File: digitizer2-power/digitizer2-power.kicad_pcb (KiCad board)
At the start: 2 copper layers, 25 x 40 mm, 37 parts, among them P1 CONN_01X02, P2 CONN_01X05, Q1 Q_NPN_BEC, Q2 Q_NPN_BEC, U1 LM3674, U2 LM3671MF-1.8, U3 LM3671MF-1.5, U4 LM3671MF-3.3

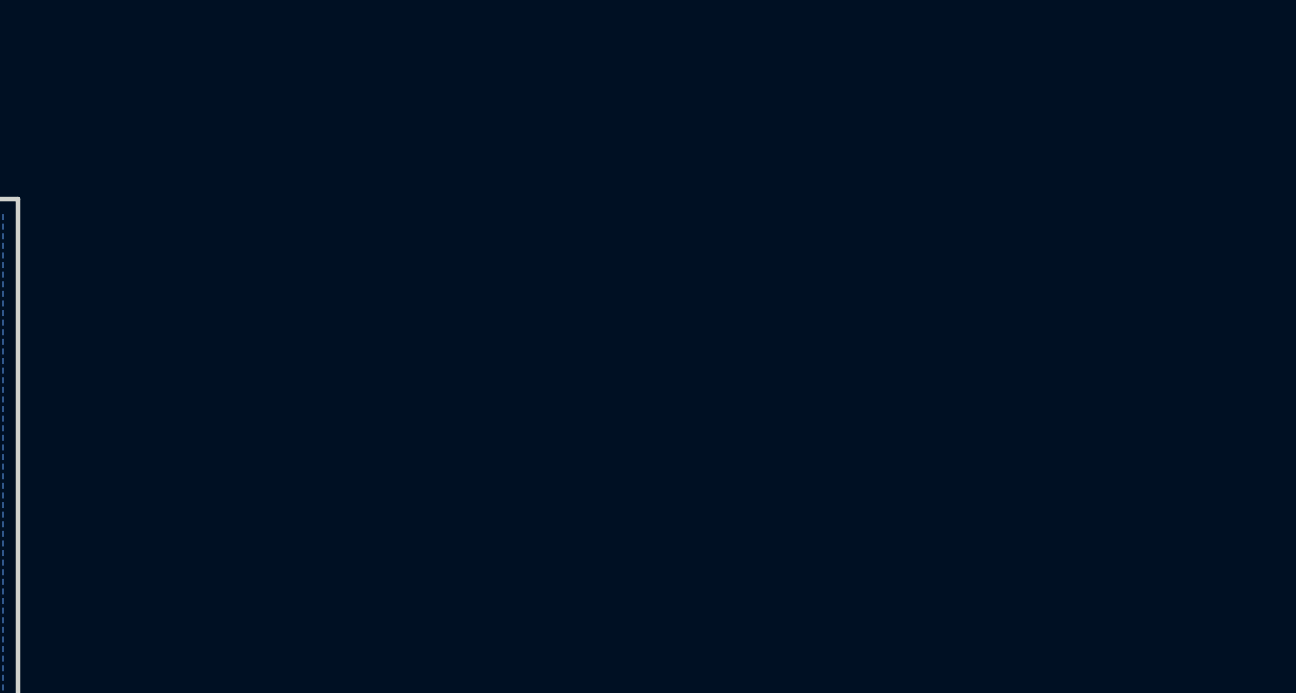
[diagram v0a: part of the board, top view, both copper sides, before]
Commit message: Add buck module project for new power supply
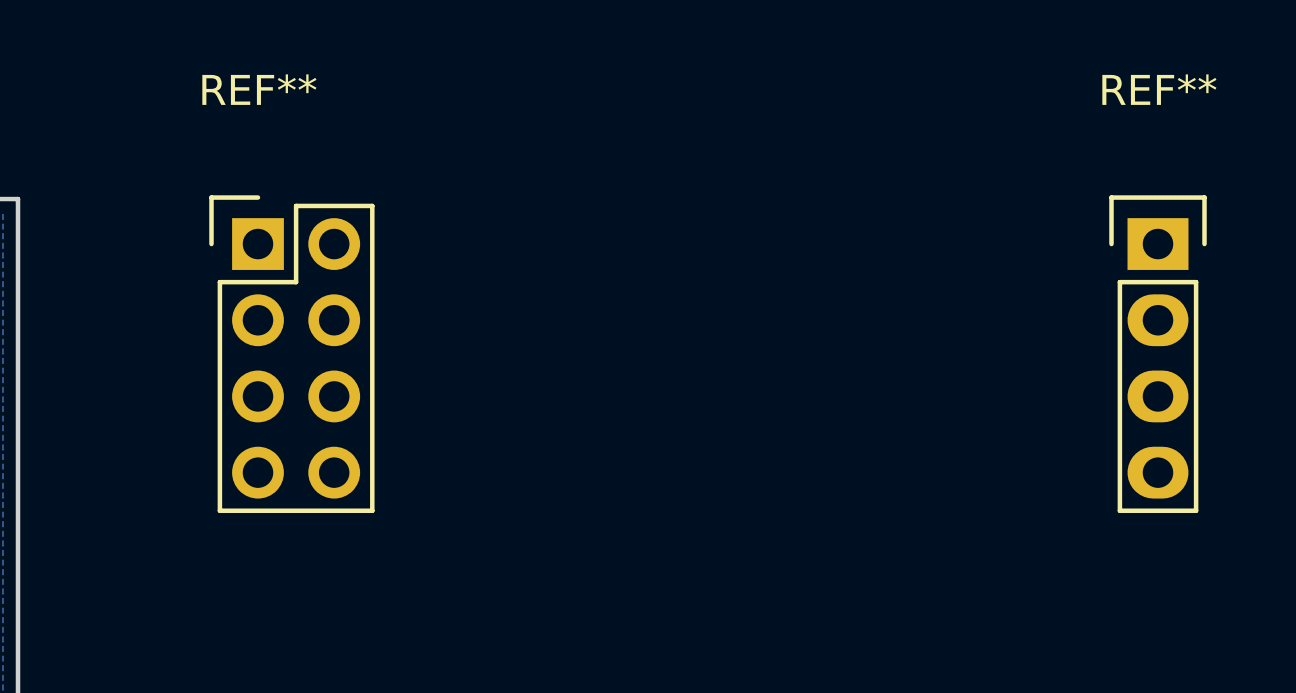
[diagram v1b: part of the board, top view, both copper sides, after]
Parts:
- added REF**: Pin_Header_Straight_1x04, Pin_Headers:Pin_Header_Straight_1x04, F.Cu at (220.0, 87.5)
- added REF**: Pin_Header_Straight_2x04, Pin_Headers:Pin_Header_Straight_2x04, F.Cu at (190.0, 87.5)
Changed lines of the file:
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@@
 (kicad_pcb (version 4) (host pcbnew 4.0.2+e4-6225~38~ubuntu16.04.1-stable)
   (general
-    (links 75)
+    (links 0)
     (no_connects 1)
     (area 155.891667 85.924999 188.325002 126.075001)
@@
     (tracks 300)
     (zones 0)
-    (modules 37)
+    (modules 39)
     (nets 17)
   )
@@
     )
   )
+  (module Pin_Headers:Pin_Header_Straight_1x04 (layer F.Cu)
+    (at 220 87.5)
+    (descr "Through hole pin header")
+    (tags "pin header")
+    (fp_text reference REF** (at 0 -5.1) (layer F.SilkS)
+      (effects (font (size 1 1) (thickness 0.15)))
+    )
+    (fp_text value Pin_Header_Straight_1x04 (at 0 -3.1) (layer F.Fab)
+      (effects (font (size 1 1) (thickness 0.15)))
+    )
+    (fp_line (start -1.75 -1.75) (end -1.75 9.4) (layer F.CrtYd) (width 0.05))
+    (fp_line (start 1.75 -1.75) (end 1.75 9.4) (layer F.CrtYd) (width 0.05))
+    (fp_line (start -1.75 -1.75) (end 1.75 -1.75) (layer F.CrtYd) (width 0.05))
+    (fp_line (start -1.75 9.4) (end 1.75 9.4) (layer F.CrtYd) (width 0.05))
+    (fp_line (start -1.27 1.27) (end -1.27 8.89) (layer F.SilkS) (width 0.15))
+    (fp_line (start 1.27 1.27) (end 1.27 8.89) (layer F.SilkS) (width 0.15))
+    (fp_line (start 1.55 -1.55) (end 1.55 0) (layer F.SilkS) (width 0.15))
+    (fp_line (start -1.27 8.89) (end 1.27 8.89) (layer F.SilkS) (width 0.15))
+    (fp_line (start 1.27 1.27) (end -1.27 1.27) (layer F.SilkS) (width 0.15))
+    (fp_line (start -1.55 0) (end -1.55 -1.55) (layer F.SilkS) (width 0.15))
+    (fp_line (start -1.55 -1.55) (end 1.55 -1.55) (layer F.SilkS) (width 0.15))
+    (pad 1 thru_hole rect (at 0 0) (size 2.032 1.7272) (drill 1.016) (layers *.Cu *.Mask F.SilkS))
+    (pad 2 thru_hole oval (at 0 2.54) (size 2.032 1.7272) (drill 1.016) (layers *.Cu *.Mask F.SilkS))
+    (pad 3 thru_hole oval (at 0 5.08) (size 2.032 1.7272) (drill 1.016) (layers *.Cu *.Mask F.SilkS))
+    (pad 4 thru_hole oval (at 0 7.62) (size 2.032 1.7272) (drill 1.016) (layers *.Cu *.Mask F.SilkS))
+    (model Pin_Headers.3dshapes/Pin_Header_Straight_1x04.wrl
+      (at (xyz 0 -0.15 0))
+      (scale (xyz 1 1 1))
+      (rotate (xyz 0 0 90))
+    )
+  )
+  (module Pin_Headers:Pin_Header_Straight_2x04 (layer F.Cu)
+    (at 190 87.5)
+    (descr "Through hole pin header")
+    (tags "pin header")
+    (fp_text reference REF** (at 0 -5.1) (layer F.SilkS)
+      (effects (font (size 1 1) (thickness 0.15)))
+    )
+    (fp_text value Pin_Header_Straight_2x04 (at 0 -3.1) (layer F.Fab)
+      (effects (font (size 1 1) (thickness 0.15)))
+    )
+    (fp_line (start -1.75 -1.75) (end -1.75 9.4) (layer F.CrtYd) (width 0.05))
+    (fp_line (start 4.3 -1.75) (end 4.3 9.4) (layer F.CrtYd) (width 0.05))
+    (fp_line (start -1.75 -1.75) (end 4.3 -1.75) (layer F.CrtYd) (width 0.05))
+    (fp_line (start -1.75 9.4) (end 4.3 9.4) (layer F.CrtYd) (width 0.05))
+    (fp_line (start -1.27 1.27) (end -1.27 8.89) (layer F.SilkS) (width 0.15))
+    (fp_line (start -1.27 8.89) (end 3.81 8.89) (layer F.SilkS) (width 0.15))
+    (fp_line (start 3.81 8.89) (end 3.81 -1.27) (layer F.SilkS) (width 0.15))
+    (fp_line (start 3.81 -1.27) (end 1.27 -1.27) (layer F.SilkS) (width 0.15))
+    (fp_line (start 0 -1.55) (end -1.55 -1.55) (layer F.SilkS) (width 0.15))
+    (fp_line (start 1.27 -1.27) (end 1.27 1.27) (layer F.SilkS) (width 0.15))
+    (fp_line (start 1.27 1.27) (end -1.27 1.27) (layer F.SilkS) (width 0.15))
+    (fp_line (start -1.55 -1.55) (end -1.55 0) (layer F.SilkS) (width 0.15))
+    (pad 1 thru_hole rect (at 0 0) (size 1.7272 1.7272) (drill 1.016) (layers *.Cu *.Mask F.SilkS))
+    (pad 2 thru_hole oval (at 2.54 0) (size 1.7272 1.7272) (drill 1.016) (layers *.Cu *.Mask F.SilkS))
+    (pad 3 thru_hole oval (at 0 2.54) (size 1.7272 1.7272) (drill 1.016) (layers *.Cu *.Mask F.SilkS))
+    (pad 4 thru_hole oval (at 2.54 2.54) (size 1.7272 1.7272) (drill 1.016) (layers *.Cu *.Mask F.SilkS))
+    (pad 5 thru_hole oval (at 0 5.08) (size 1.7272 1.7272) (drill 1.016) (layers *.Cu *.Mask F.SilkS))
+    (pad 6 thru_hole oval (at 2.54 5.08) (size 1.7272 1.7272) (drill 1.016) (layers *.Cu *.Mask F.SilkS))
+    (pad 7 thru_hole oval (at 0 7.62) (size 1.7272 1.7272) (drill 1.016) (layers *.Cu *.Mask F.SilkS))
+    (pad 8 thru_hole oval (at 2.54 7.62) (size 1.7272 1.7272) (drill 1.016) (layers *.Cu *.Mask F.SilkS))
+    (model Pin_Headers.3dshapes/Pin_Header_Straight_2x04.wrl
+      (at (xyz 0.05 -0.15 0))
+      (scale (xyz 1 1 1))
+      (rotate (xyz 0 0 90))
+    )
+  )

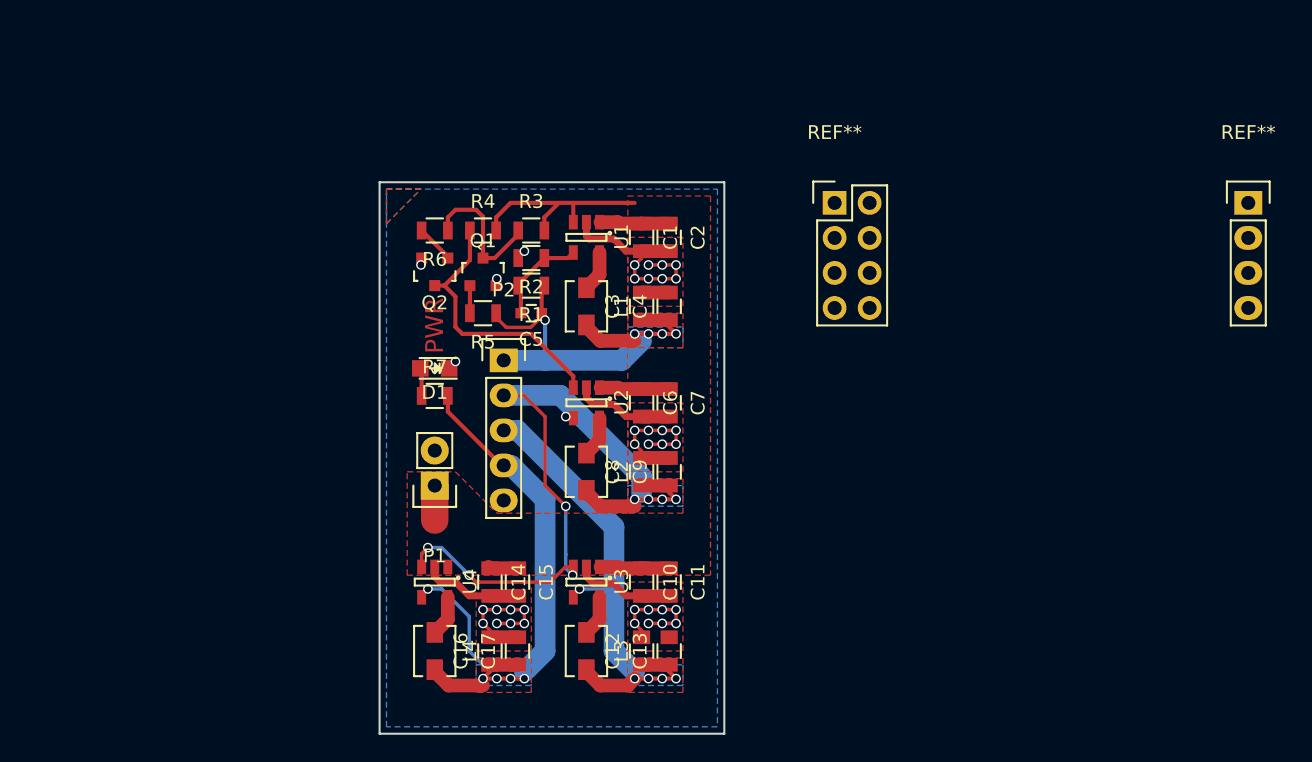
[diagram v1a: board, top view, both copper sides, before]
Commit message: Build new digitizer2-power board from buck module
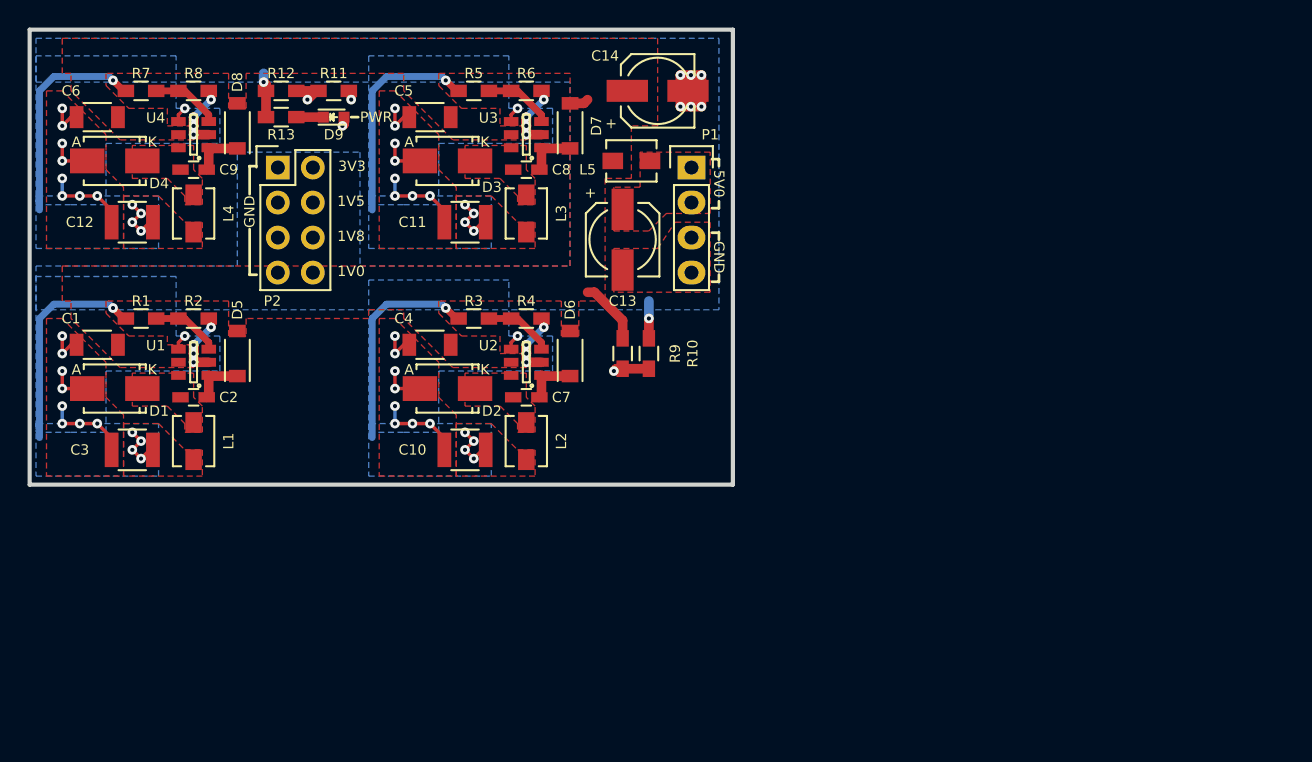
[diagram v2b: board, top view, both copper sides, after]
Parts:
- removed C15, C16, C17: 4.7uF, Capacitors_SMD:C_0805
- removed Q1, Q2: Q_NPN_BEC, TO_SOT_Packages_SMD:SOT-23
- removed REF**: Pin_Header_Straight_1x04, Pin_Headers:Pin_Header_Straight_1x04
- removed REF**: Pin_Header_Straight_2x04, Pin_Headers:Pin_Header_Straight_2x04
- added D2: D_Schottky_Small, Diodes_SMD:SMA_Standard, F.Cu at (161.9, 101.0)
- added D3: D_Schottky_Small, Diodes_SMD:SMA_Standard, F.Cu at (161.9, 84.5)
- added D4: D_Schottky_Small, Diodes_SMD:SMA_Standard, F.Cu at (137.8, 84.5)
- added D5: D_Schottky_Small, Diodes_SMD:SOD-123, F.Cu at (146.7, 98.4)
- added D6: D_Schottky_Small, Diodes_SMD:SOD-123, F.Cu at (170.8, 98.4)
- added D7: D_Schottky_Small, Diodes_SMD:SOD-123, F.Cu at (170.8, 81.9)
- added D8: D_Schottky_Small, Diodes_SMD:SOD-123, F.Cu at (146.7, 81.9)
- added D9: 1.8V, LEDs:LED_0603, F.Cu at (153.7, 81.3)
- added L5: 2.2uH, digitizer2_modules:IHLP-1212BZ-11, F.Cu at (175.3, 84.5)
- added R10: Ren2, Resistors_SMD:R_0603_HandSoldering, F.Cu at (176.5, 98.4)
- added R11: Ren1, Resistors_SMD:R_0603_HandSoldering, F.Cu at (153.7, 79.4)
- added R12: Ren2, Resistors_SMD:R_0603_HandSoldering, F.Cu at (149.9, 79.4)
- added R13: 750, Resistors_SMD:R_0603_HandSoldering, F.Cu at (149.9, 81.3)
- added R8: div2, Resistors_SMD:R_0603_HandSoldering, F.Cu at (143.5, 79.4)
- added R9: Ren1, Resistors_SMD:R_0603_HandSoldering, F.Cu at (174.6, 98.4)
- C1, C4, C6: value 4.7uF -> 10uF; footprint Capacitors_SMD:C_0805 -> Capacitors_SMD:C_1206
- C10, C11, C12, C3: value 4.7uF -> C_Small; footprint Capacitors_SMD:C_0805 -> Capacitors_SMD:C_1210
- C13, C14: value 4.7uF -> C_Small; footprint Capacitors_SMD:C_0805 -> Capacitors_SMD:c_elec_5x5.7
- C2, C7, C8, C9: value 4.7uF -> 0.1uF; footprint Capacitors_SMD:C_0805 -> Capacitors_SMD:C_0603_HandSoldering
- C5: value 18pF -> 10uF; footprint Capacitors_SMD:C_0603 -> Capacitors_SMD:C_1206
- D1: value LED -> D_Schottky_Small; footprint LEDs:LED_0805 -> Diodes_SMD:SMA_Standard
- P1: value CONN_01X02 -> CONN_01X04; footprint Pin_Headers:Pin_Header_Straight_1x02 -> Pin_Headers:Pin_Header_Straight_1x04
- P2: value CONN_01X05 -> CONN_02X04; footprint Pin_Headers:Pin_Header_Straight_1x05 -> Pin_Headers:Pin_Header_Straight_2x04
- R1: value 200k -> div1; footprint Resistors_SMD:R_0805 -> Resistors_SMD:R_0603_HandSoldering
- R2: value 200k -> div2; footprint Resistors_SMD:R_0805 -> Resistors_SMD:R_0603_HandSoldering
- R3: value 10k -> div1; footprint Resistors_SMD:R_0805 -> Resistors_SMD:R_0603_HandSoldering
- R4: value 10k -> div2; footprint Resistors_SMD:R_0805 -> Resistors_SMD:R_0603_HandSoldering
- R5: value 1k -> div1; footprint Resistors_SMD:R_0805 -> Resistors_SMD:R_0603_HandSoldering
- R6: value 1k -> div2; footprint Resistors_SMD:R_0805 -> Resistors_SMD:R_0603_HandSoldering
- R7: value 600 -> div1; footprint Resistors_SMD:R_0805 -> Resistors_SMD:R_0603_HandSoldering
- U1: value LM3674 -> ADP2301; footprint TO_SOT_Packages_SMD:SOT-23-5 -> TO_SOT_Packages_SMD:SOT-23-6
- U2: value LM3671MF-1.8 -> ADP2301; footprint TO_SOT_Packages_SMD:SOT-23-5 -> TO_SOT_Packages_SMD:SOT-23-6
- U3: value LM3671MF-1.5 -> ADP2301; footprint TO_SOT_Packages_SMD:SOT-23-5 -> TO_SOT_Packages_SMD:SOT-23-6
- U4: value LM3671MF-3.3 -> ADP2301; footprint TO_SOT_Packages_SMD:SOT-23-5 -> TO_SOT_Packages_SMD:SOT-23-6
- moved C12 48.3 mm to (139.1, 88.9), turned to 180 degrees
- moved C6 44.6 mm to (136.5, 81.3), turned to 180 degrees
- moved C9 40.9 mm to (143.5, 85.1), turned to 180 degrees
- moved C1 40.2 mm to (136.5, 97.8), turned to 180 degrees
- moved C3 38.4 mm to (139.1, 105.4), turned to 180 degrees
- moved C14 37.6 mm to (177.2, 79.4), turned to 0 degrees
- moved U4 36.9 mm to (143.5, 82.5), turned to 180 degrees
- moved C2 36.4 mm to (143.5, 101.6), turned to 180 degrees
- moved L4 36.2 mm to (143.5, 88.3)
- moved U3 32.7 mm to (167.6, 82.5), turned to 180 degrees
- moved L3 32.0 mm to (167.6, 88.3)
- moved R7 30.7 mm to (139.7, 79.4)
- moved L1 30.1 mm to (143.5, 104.8)
- moved C13 30.0 mm to (174.6, 90.2), turned to 270 degrees
- moved C11 30.0 mm to (163.2, 88.9), turned to 180 degrees
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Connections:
- C10 pad 1: /5V0 -> /1V8
- C11 pad 1: /5V0 -> /1V5
- C12 pad 1: /1V5 -> /3V3
- C13 pad 1: /1V5 -> /5V0_IN
- C2 pad 1: /5V0 -> /BST1
- C2 pad 2: GND -> /SW1
- C4 pad 1: /1V0 -> /5V0
- C5 pad 1: /1V0 -> /5V0
- C5 pad 2: Net-(C5-Pad2) -> GND
- C7 pad 1: /5V0 -> /BST2
- C7 pad 2: GND -> /SW2
- C8 pad 1: /1V8 -> /BST3
- C8 pad 2: GND -> /SW3
- C9 pad 1: /1V8 -> /BST4
- C9 pad 2: GND -> /SW4
- D1 pad 1: GND -> /SW1
- D1 pad 2: Net-(D1-Pad2) -> GND
- L1 pad 1: Net-(L1-Pad1) -> /SW1
- L2 pad 1: Net-(L2-Pad1) -> /SW2
- L3 pad 1: Net-(L3-Pad1) -> /SW3
- L4 pad 1: Net-(L4-Pad1) -> /SW4
- P1 pad 1: /5V0 -> /5V0_IN
- P1 pad 2: GND -> /5V0_IN
- P2 pad 1: /1V0 -> GND
- P2 pad 2: /1V8 -> /3V3
- P2 pad 3: /1V5 -> GND
- P2 pad 4: /3V3 -> /1V5
- R1 pad 2: Net-(C5-Pad2) -> /FB1
- R2 pad 1: Net-(C5-Pad2) -> /FB1
- R3 pad 1: Net-(Q1-Pad3) -> /1V8
- R3 pad 2: /5V0 -> /FB2
- R4 pad 1: /1V0_ENABLED -> /FB2
- R4 pad 2: /5V0 -> GND
- R5 pad 1: /1V0 -> /1V5
- R5 pad 2: Net-(Q1-Pad1) -> /FB3
- R6 pad 1: Net-(Q1-Pad3) -> /FB3
- R6 pad 2: Net-(Q2-Pad1) -> GND
- R7 pad 1: Net-(D1-Pad2) -> /3V3
- R7 pad 2: /3V3 -> /FB4
- U1 pad 1: /5V0 -> /BST1
- U1 pad 3: /5V0 -> /FB1
- U1 pad 4: Net-(C5-Pad2) -> /5V0
- U1 pad 5: Net-(L1-Pad1) -> /5V0
- U2 pad 1: /5V0 -> /BST2
- U2 pad 3: /1V0_ENABLED -> /FB2
- U2 pad 4: /1V8 -> /EN1V8
- U2 pad 5: Net-(L2-Pad1) -> /5V0
- U3 pad 1: /5V0 -> /BST3
- U3 pad 3: /1V8 -> /FB3
- U3 pad 4: /1V5 -> /PGOOD1V8
- U3 pad 5: Net-(L3-Pad1) -> /5V0
- U4 pad 1: /5V0 -> /BST4
- U4 pad 3: /1V8 -> /FB4
- U4 pad 4: /3V3 -> /PGOOD1V8
- U4 pad 5: Net-(L4-Pad1) -> /5V0
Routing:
- net /1V8: track 56.4 -> 95.7 mm, vias 9 -> 6
- net /PGOOD1V8: track 0.00 -> 31.3 mm, vias 0 -> 3
- net /5V0: track 35.0 -> 7.37 mm, vias 0 -> 1
- net (no net): track 19.7 -> 0.00 mm
- net /1V0_ENABLED: track 19.7 -> 0.00 mm
- net GND: track 70.8 -> 85.6 mm, vias 36 -> 56
- net /EN1V8: track 0.00 -> 14.4 mm, vias 0 -> 2
- net Net-(Q1-Pad3): track 10.5 -> 0.00 mm
- net /1V0: track 30.7 -> 40.5 mm
- net Net-(C5-Pad2): track 7.14 -> 0.00 mm
- net /FB4: track 0.00 -> 5.02 mm
- net /FB3: track 0.00 -> 5.02 mm
- net /FB2: track 0.00 -> 5.02 mm
- net /FB1: track 0.00 -> 5.02 mm
- net /BST4: track 0.00 -> 3.75 mm
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- added copper zone on In1.Cu, net /1V0
- added copper zone on In1.Cu, net /1V5
- added copper zone on In1.Cu, net /1V8
- added copper zone on In1.Cu, net /3V3
- added copper zone on F.Cu, net /5V0_IN
- added copper zone on F.Cu, net /SW1
- added copper zone on F.Cu, net /SW2
- added copper zone on F.Cu, net /SW3
- added copper zone on F.Cu, net /SW4
- added copper zone on In2.Cu, net GND
- removed copper zone on B.Cu, net (none)
- removed copper zone on F.Cu, net (none)
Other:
- board size 25 x 40 mm -> 51 x 33 mm
- copper layers 2 -> 4
- net class Default: via_drill 0.5 -> 0.3
- rule pad_to_mask_clearance: 0.05 -> 0
- rule via_min_drill: 0.5 -> 0.3
- rule via_min_size: 0.7 -> 0.4
- board text added: "1V0"
- board text added: "1V5"
- board text added: "1V8"
- board text added: "3V3"
- board text added: "5V0"
- board text added: "GND"
